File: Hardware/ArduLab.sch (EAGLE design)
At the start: 94 parts, among them CN1 USB-B, CN2 JST-PH, T1 MMUN2133LT1G, U1 ATMEGA32U4-AU, U2 MIC5205, U3 TPS61030PWP, U4 MCP73831, U5 L293DD, X1 16MHz

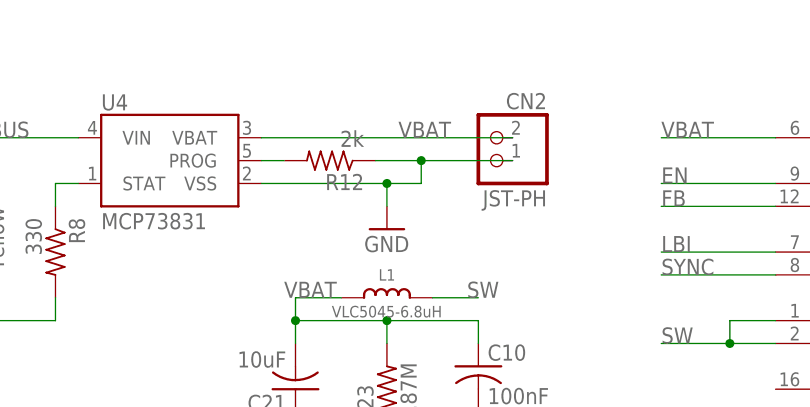
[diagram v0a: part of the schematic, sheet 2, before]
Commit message: Fixed bug: Battery connector polarity
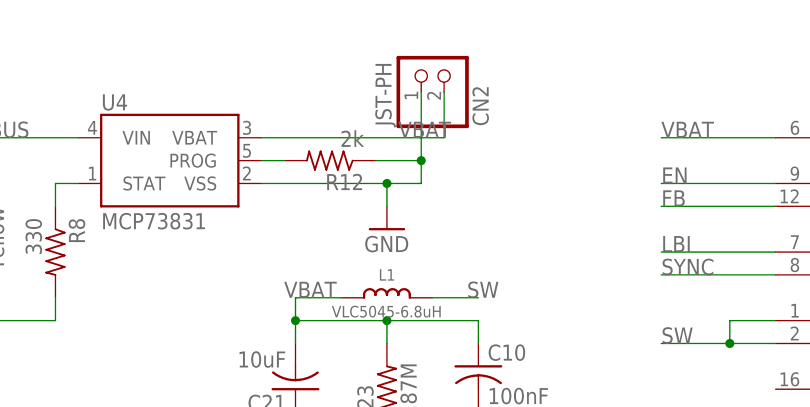
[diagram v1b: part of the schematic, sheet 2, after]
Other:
- moved on the sheet: CN2
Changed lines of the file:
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@@
 <attribute name="VALUE" x="191.77" y="138.43" size="1.778" layer="96" rot="R90"/>
 </instance>
-<instance part="CN2" gate="G$1" x="88.9" y="157.48" rot="MR0"/>
+<instance part="CN2" gate="G$1" x="81.28" y="167.64" rot="MR90"/>
 <instance part="C25" gate="G$1" x="222.25" y="165.1"/>
 <instance part="R7" gate="G$1" x="241.3" y="149.86" rot="R90"/>
@@
 <junction x="77.47" y="154.94"/>
 <pinref part="CN2" gate="G$1" pin="2"/>
-<wire x1="91.44" y1="157.48" x2="81.28" y2="157.48" width="0.1524" layer="91"/>
+<wire x1="81.28" y1="165.1" x2="81.28" y2="157.48" width="0.1524" layer="91"/>
 <junction x="81.28" y="157.48"/>
 </segment>
@@
 <pinref part="CN2" gate="G$1" pin="1"/>
 <pinref part="U4" gate="G$1" pin="VBAT"/>
-<wire x1="91.44" y1="160.02" x2="63.5" y2="160.02" width="0.1524" layer="91"/>
+<wire x1="83.82" y1="165.1" x2="83.82" y2="160.02" width="0.1524" layer="91"/>
+<wire x1="83.82" y1="160.02" x2="63.5" y2="160.02" width="0.1524" layer="91"/>
 <label x="78.74" y="160.02" size="1.778" layer="95"/>
 </segment>

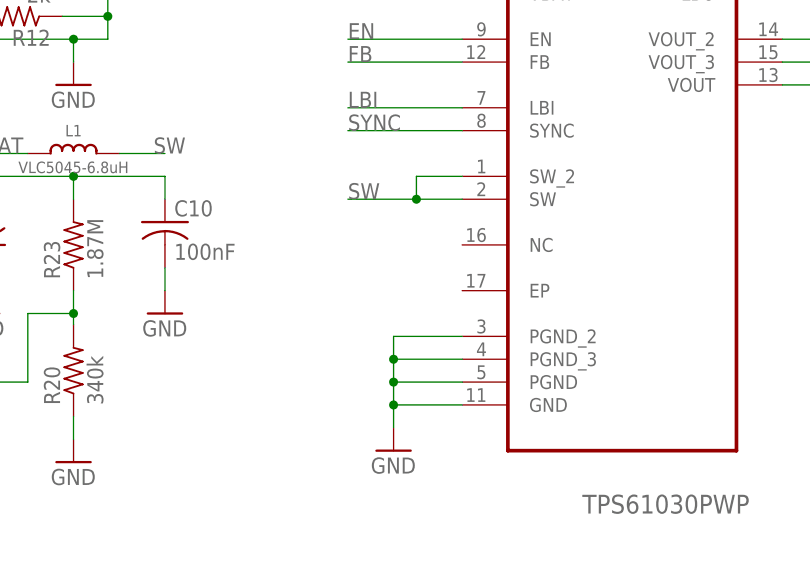
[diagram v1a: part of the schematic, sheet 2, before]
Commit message: Modified: Center pad of U3 (TPS61030) wired to ground
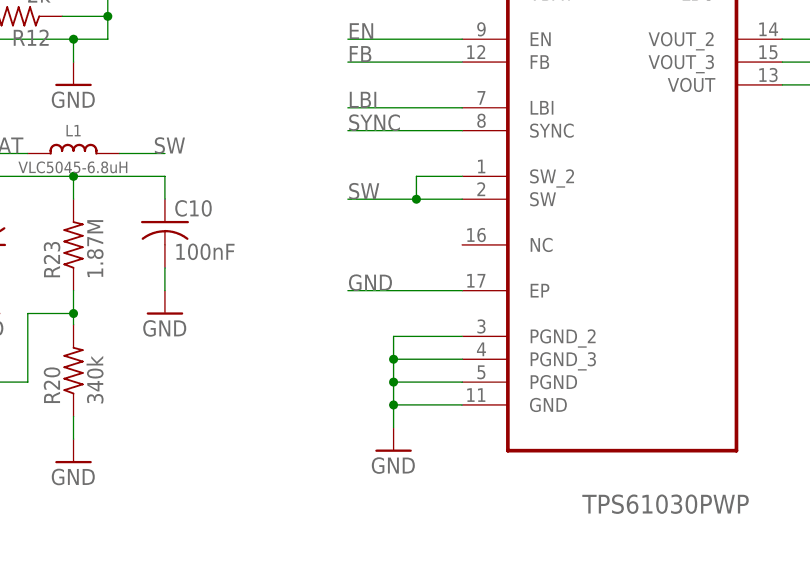
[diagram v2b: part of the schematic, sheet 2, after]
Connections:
- net GND: now also U3.EP
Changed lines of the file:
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@@
 <setting verticaltext="up"/>
 </settings>
-<grid distance="0.1" unitdist="inch" unit="inch" style="lines" multiple="1" display="no" altdistance="0.01" altunitdist="inch" altunit="inch"/>
+<grid distance="0.05" unitdist="inch" unit="inch" style="lines" multiple="1" display="no" altdistance="0.01" altunitdist="inch" altunit="inch"/>
 <layers>
 <layer number="1" name="Top" color="4" fill="1" visible="no" active="no"/>
@@
 <wire x1="67.31" y1="129.54" x2="67.31" y2="127" width="0.1524" layer="91"/>
 </segment>
-</net>
+<segment>
+<wire x1="120.65" y1="127" x2="107.95" y2="127" width="0.1524" layer="91"/>
+<label x="107.95" y="127" size="1.778" layer="95"/>
+<pinref part="U3" gate="A" pin="EP"/>
+</segment>
+</net>

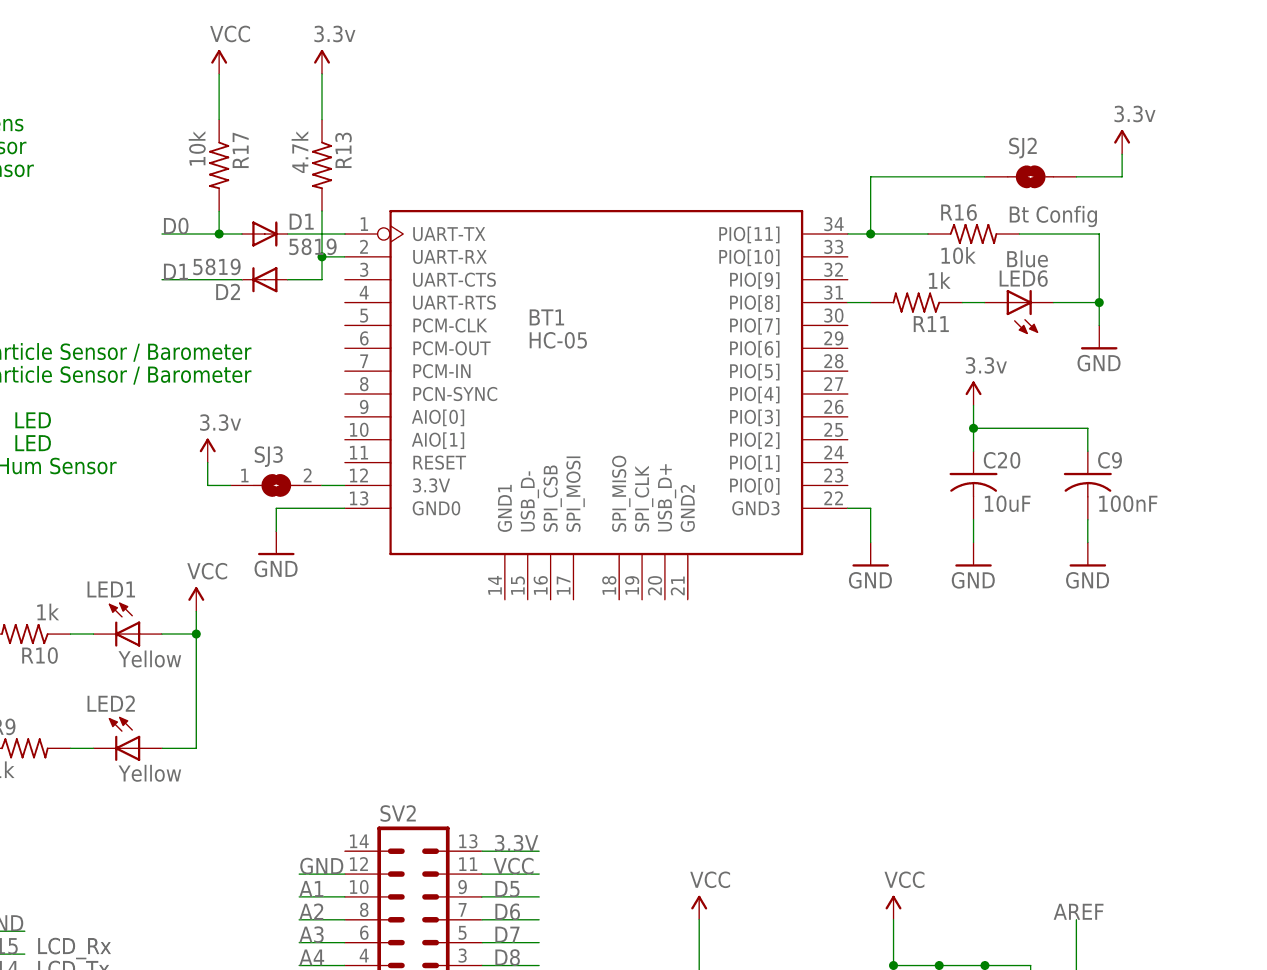
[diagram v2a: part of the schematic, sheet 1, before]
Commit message: Bluetooth-microcontroller communication improved with shift level conversor.
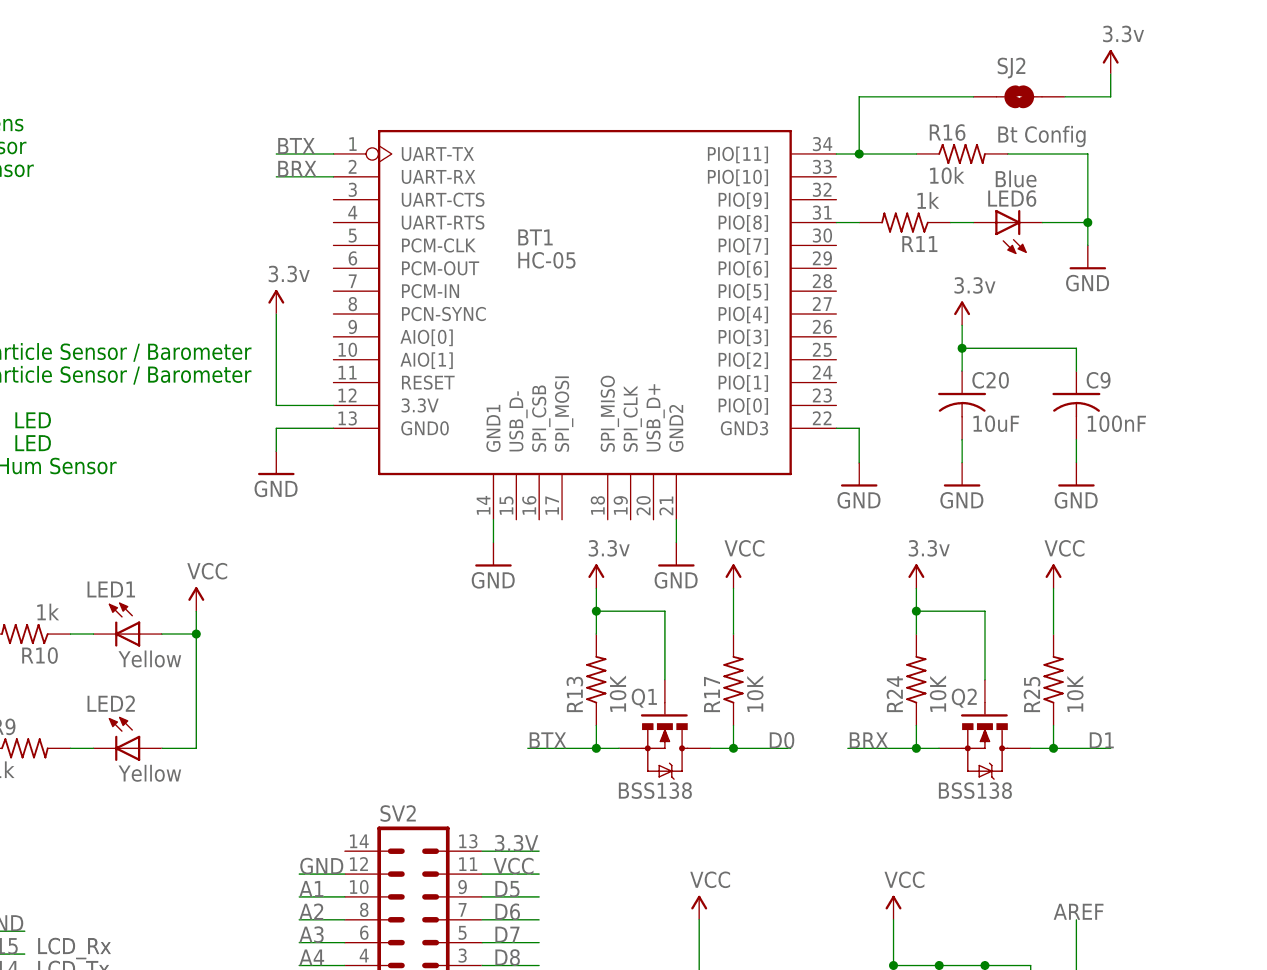
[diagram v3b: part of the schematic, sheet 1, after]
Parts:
- removed D1, D2: 5819, diode:DIODE-SOD123
- removed SJ3: (no value), jumper:SJ
- added Q1, Q2: BSS138, SparkFun:MOSFET-NCHANNELSMD
- added R24, R25: 10K, resistor:R-US_R1206
- R13: value 4.7k -> 10K
- R17: value 10k -> 10K
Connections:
- removed net N$20: BT1.UART-TX, D1.C
- removed net N$21: BT1.UART-RX, D2.A, R13.2
- removed net N$7: BT1.3.3V, SJ3.2
- new net BRX: BT1.UART-RX, Q2.S, R24.1
- new net BTX: BT1.UART-TX, Q1.S, R13.1
- net 3.3V: now also BT1.3.3V, Q1.G, Q2.G, R13.2, R24.2; no longer R13.1, SJ3.1
- net D0: now also Q1.D, R17.1; no longer D1.A, R17.2
- net D1: now also Q2.D, R25.1; no longer D2.C
- net GND: now also BT1.GND1, BT1.GND2
- net VCC: now also R17.2, R25.2; no longer R17.1
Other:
- moved on the sheet: BT1, C20, C9, LED6, R11, R13, R16, R17, SJ2

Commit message: Added support for ESP8266-01
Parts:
- added U$1: ESP01, esp8266modules:ESP01
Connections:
- removed net BRX: BT1.UART-RX, Q2.S, R24.1
- removed net BTX: BT1.UART-TX, Q1.S, R13.1
- removed net N$18: BT1.PIO[8], R11.2
- removed net N$24: BT1.PIO[11], R16.1, SJ2.1
- new net CL: BT1.PIO[8], R11.2, U$1.GPIO0
- new net CONF: BT1.PIO[11], R16.1, SJ2.1, U$1.RST
- new net RX: BT1.UART-RX, Q2.S, R24.1, U$1.RXD
- new net TX: BT1.UART-TX, Q1.S, R13.1, U$1.TXD
- net 3.3V: now also U$1.CH_PD, U$1.VCC
- net GND: now also U$1.GND
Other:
- moved on the sheet: C18, C19, C3, C4, C5, C6, C7, C8, CN1, H1, H2, H3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

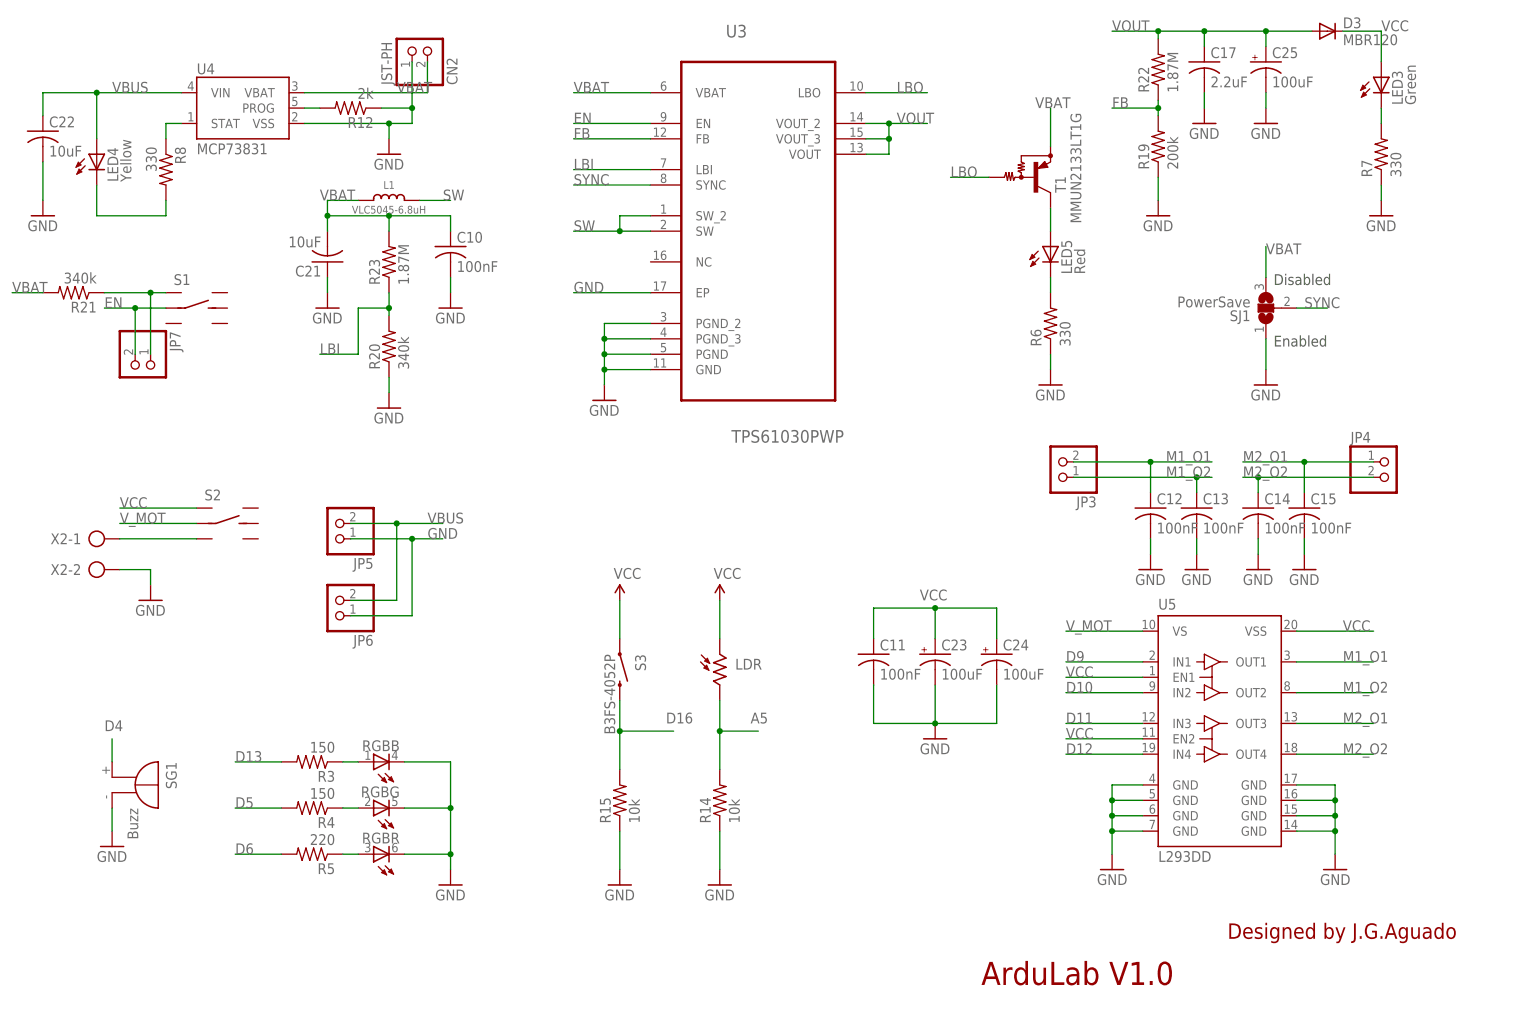
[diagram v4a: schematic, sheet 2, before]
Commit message: LiPo power boosting circuit based in PAM2401 IC
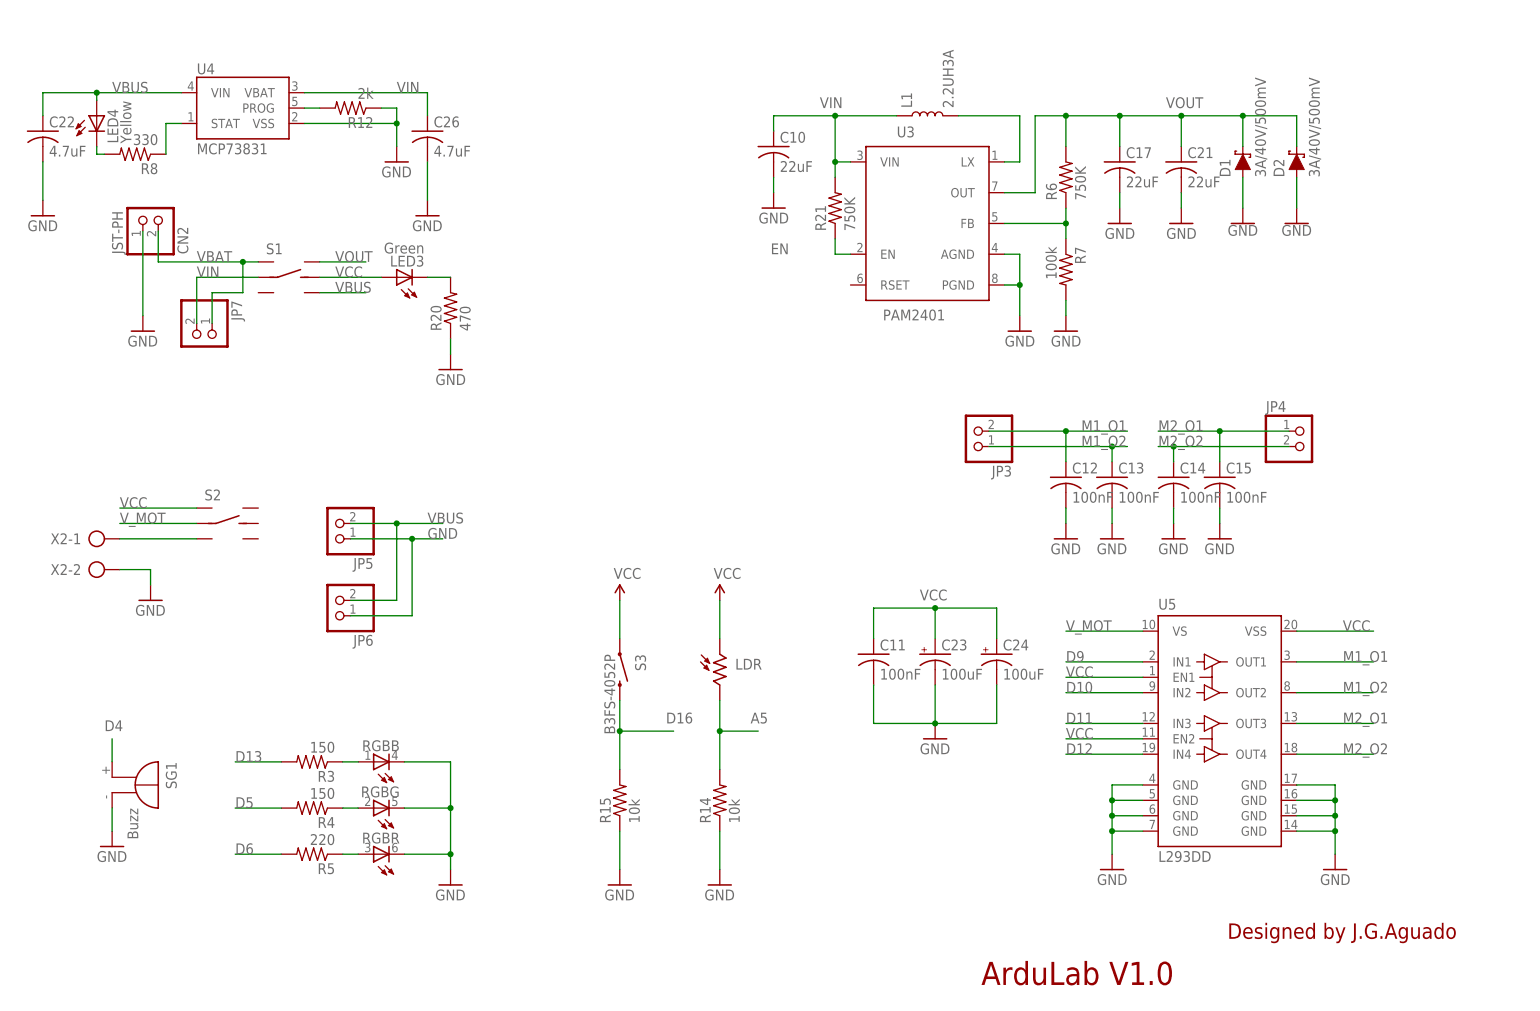
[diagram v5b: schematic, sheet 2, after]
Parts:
- removed C25: 100uF, SparkFun:CAP_POL3528-KIT
- removed D3: MBR120, diode:DIODE-SOD123
- removed LED5: Red, led:LEDSMT1206
- removed R19: 200k, resistor:R-US_R1206
- removed R22, R23: 1.87M, resistor:R-US_R1206
- removed SJ1: PowerSave, jumper:SJ2W
- removed T1: MMUN2133LT1G, transistor:MUN2114T1-PNP_DRIVER-SC59-BEC
- added C26: 4.7uF, resistor:C-USC1206
- added D1, D2: 3A/40V/500mV, SparkFun-DiscreteSemi:DIODE-SCHOTTKY-B340A
- C10: value 100nF -> 22uF
- C17: value 2.2uF -> 22uF
- C21: value 10uF -> 22uF
- C22: value 10uF -> 4.7uF
- L1: value VLC5045-6.8uH -> 2.2UH3A; device microbuilder:INDUCTORTDK_VLC5045 -> SparkFun-Coils:INDUCTOR-IFSC1515AHER2R2M01
- R20: value 340k -> 470
- R21: value 340k -> 750K
- R6: value 330 -> 750K
- R7: value 330 -> 100k
- U3: value TPS61030PWP -> PAM2401; device Texas Instruments_By_element14_Batch_1:TPS61030PWP -> SparkFun-IC-Power:PAM2401
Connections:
- removed net FB: R19.2, R22.1, U3.FB
- removed net LBI: R20.2, R23.1, U3.LBI
- removed net LBO: T1.B, U3.LBO
- removed net N$17: LED3.C, R7.2
- removed net N$3: LED5.C, R6.2
- removed net SW: L1.2, U3.SW, U3.SW_2
- removed net SYNC: SJ1.2, U3.SYNC
- new net N$14: LED3.C, R20.2
- new net VIN: C10.1, C26.1, JP7.2, L1.1, R21.2, S1.LC, U3.VIN, U4.VBAT
- net EN: now also R21.1; no longer JP7.2, S1.LC
- net GND: now also C21.2, C26.2, D1.A, D2.A, R7.2, U3.AGND; no longer C21.1, C25.-, R19.1, R6.1, R7.1, SJ1.1, U3.EP, U3.GND, U3.PGND_2, U3.PGND_3
- net N$1: now also R6.1, R7.1, U3.FB; no longer JP7.1, R21.1, S1.L1
- net N$4: now also L1.2, U3.LX; no longer LED5.A, T1.C
- net VBAT: now also JP7.1, S1.L1; no longer C10.1, C21.2, L1.1, R21.2, R23.2, SJ1.3, T1.E, U3.VBAT, U4.VBAT
- net VBUS: now also S1.R2
- net VCC: now also S1.RC; no longer D3.C
- net VOUT: now also C21.1, D1.C, D2.C, R6.2, S1.R1, U3.OUT; no longer C25.+, D3.A, R22.2, U3.VOUT, U3.VOUT_2, U3.VOUT_3
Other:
- note removed: "Disabled"
- note removed: "Enabled"
- moved on the sheet: C10, C12, C13, C14, C15, C17, C21, CN2, JP3, JP4, JP7, LED3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

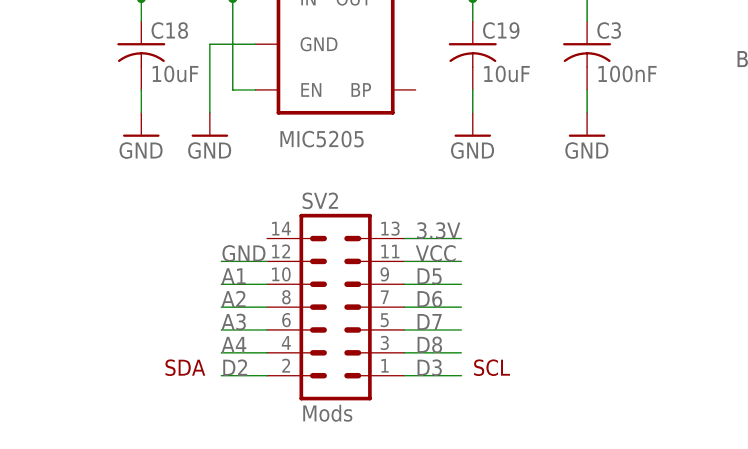
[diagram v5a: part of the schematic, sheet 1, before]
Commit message: Added support for Serial interface in Mod connector
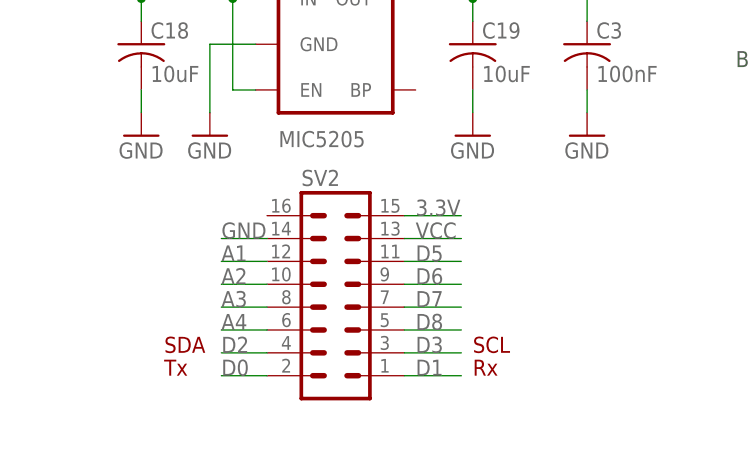
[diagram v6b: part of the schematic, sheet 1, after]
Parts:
- SV2: value Mods -> (none); device con-lstb:MA07-2 -> con-lstb:MA08-2
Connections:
- net 3.3V: now also SV2.15; no longer SV2.13
- net A1: now also SV2.12; no longer SV2.10
- net A2: now also SV2.10; no longer SV2.8
- net A3: now also SV2.8; no longer SV2.6
- net A4: now also SV2.6; no longer SV2.4
- net D0: now also SV2.2
- net D1: now also SV2.1
- net D2: now also SV2.4; no longer SV2.2
- net D3: now also SV2.3; no longer SV2.1
- net D5: now also SV2.11; no longer SV2.9
- net D6: now also SV2.9; no longer SV2.7
- net D7: now also SV2.7; no longer SV2.5
- net D8: now also SV2.5; no longer SV2.3
- net GND: now also SV2.14; no longer SV2.12
- net VCC: now also SV2.13; no longer SV2.11
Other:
- note added: "Rx"
- note added: "Tx"
